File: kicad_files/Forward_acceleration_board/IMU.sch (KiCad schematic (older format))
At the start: 6 parts

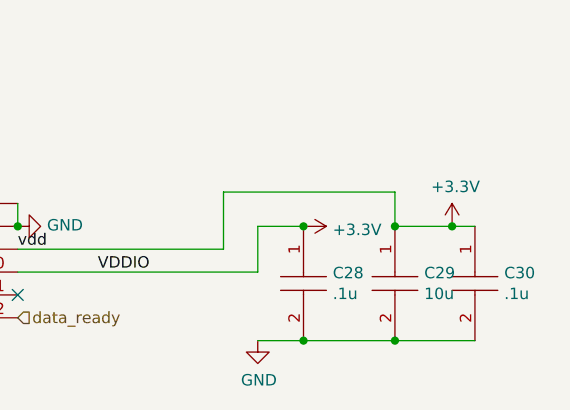
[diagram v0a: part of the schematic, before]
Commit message: updated BOMS for boards and added battery pack wiring schematic
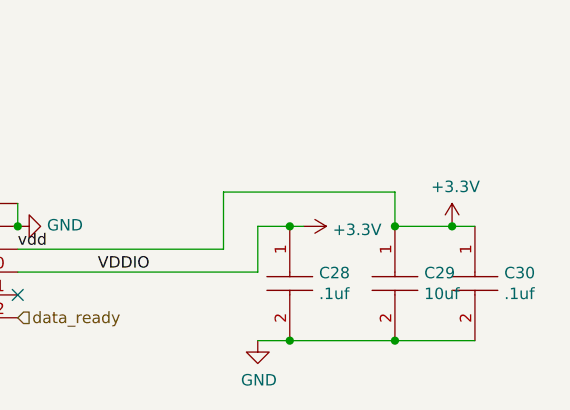
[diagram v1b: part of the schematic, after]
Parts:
- removed C28, C30: .1u, GRM155C91C105ME11J:CAPC1005X55N, symbol GRM155C80G106ME44D:GRM155C80G106ME44D
- removed C29: 10u, AS0805KKX7R0BB104:CAPC2012X145N, symbol AS0805KKX7R0BB104:AS0805KKX7R0BB104
- added C28, C30: .1uf, GRM155C91C105ME11J:CAPC1005X55N, symbol GRM155R62A104KE14D:GRM155R62A104KE14D
- added C29: 10uf, AS0805KKX7R0BB104:CAPC2012X145N, symbol GRM21BR61E106KA73K:GRM21BR61E106KA73K
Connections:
- net +3V3: now also C28.1, C29.1, C30.1
- net GND: now also C28.2, C29.2, C30.2
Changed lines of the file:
@@
 NoConn ~ 4550 3900
 $Comp
-L power:GND #PWR0152
+L Forward_acceleration_board-rescue:GND-power #PWR0152
 U 1 1 5D9F0090
 P 6050 3600
@@
 $EndComp
 $Comp
-L power:GND #PWR0153
+L Forward_acceleration_board-rescue:GND-power #PWR0153
 U 1 1 5D9F00CC
 P 4550 4000
@@
 data_ready
 $Comp
-L power:GND #PWR0154
+L Forward_acceleration_board-rescue:GND-power #PWR0154
 U 1 1 5DAEA2FA
 P 4550 3700
@@
 $EndComp
 $Comp
-L GRM155C80G106ME44D:GRM155C80G106ME44D C30
-U 1 1 5DAEA3F4
-P 8050 3600
-F 0 "C30" V 8254 3728 50  0000 L CNN
-F 1 ".1u" V 8345 3728 50  0000 L CNN
-F 2 "GRM155C91C105ME11J:CAPC1005X55N" H 8400 3650 50  0001 L CNN
-F 3 "https://componentsearchengine.com/Datasheets/1/GRM155C80G106ME44D.pdf" H 8400 3550 50  0001 L CNN
-F 4 "Multilayer Ceramic Capacitors MLCC - SMD/SMT 10UF      4V   20%        0402" H 8400 3450 50  0001 L CNN "Description"
-F 5 "0.55" H 8400 3350 50  0001 L CNN "Height"
-F 6 "81-GRM155C80G106ME44" H 8400 3250 50  0001 L CNN "Mouser Part Number"
-F 7 "https://www.mouser.com/Search/Refine.aspx?Keyword=81-GRM155C80G106ME44" H 8400 3150 50  0001 L CNN "Mouser Price/Stock"
-F 8 "Murata Electronics" H 8400 3050 50  0001 L CNN "Manufacturer_Name"
-F 9 "GRM155C80G106ME44D" H 8400 2950 50  0001 L CNN "Manufacturer_Part_Number"
-	1    8050 3600
-	0    1    1    0
-$EndComp
-$Comp
-L AS0805KKX7R0BB104:AS0805KKX7R0BB104 C29
-U 1 1 5DAEA659
-P 7700 3600
-F 0 "C29" V 7904 3728 50  0000 L CNN
-F 1 "10u" V 7995 3728 50  0000 L CNN
-F 2 "AS0805KKX7R0BB104:CAPC2012X145N" H 8050 3650 50  0001 L CNN
-F 3 "https://mouser.componentsearchengine.com/Datasheets/1/AS0805KKX7R0BB104.pdf" H 8050 3550 50  0001 L CNN
-F 4 "Multilayer Ceramic Capacitors MLCC - SMD/SMT 0.1uF 10% 100V AEC-Q200" H 8050 3450 50  0001 L CNN "Description"
-F 5 "1.45" H 8050 3350 50  0001 L CNN "Height"
-F 6 "YAGEO (PHYCOMP)" H 8050 3250 50  0001 L CNN "Manufacturer_Name"
-F 7 "AS0805KKX7R0BB104" H 8050 3150 50  0001 L CNN "Manufacturer_Part_Number"
-F 8 "603-AS0805KKX70BB104" H 8050 3050 50  0001 L CNN "Mouser Part Number"
-F 9 "https://www.mouser.com/Search/Refine.aspx?Keyword=603-AS0805KKX70BB104" H 8050 2950 50  0001 L CNN "Mouser Price/Stock"
-F 10 "" H 8050 2850 50  0001 L CNN "RS Part Number"
-F 11 "" H 8050 2750 50  0001 L CNN "RS Price/Stock"
-	1    7700 3600
-	0    1    1    0
-$EndComp
-$Comp
-L power:GND #PWR0155
+L Forward_acceleration_board-rescue:GND-power #PWR0155
 U 1 1 5DAEA827
 P 7100 4100
@@
 $EndComp
 Wire Wire Line
-	8050 4100 7700 4100
-Connection ~ 7700 4100
-Wire Wire Line
 	7100 3600 7100 3800
 Wire Wire Line
 	6050 3800 7100 3800
 Wire Wire Line
-	7100 3600 7300 3600
+	7100 3600 7240 3600
 Wire Wire Line
 	8050 3600 7950 3600
 $Comp
-L power:+3.3V #PWR0156
+L Forward_acceleration_board-rescue:+3.3V-power #PWR0156
 U 1 1 5DAEABD2
 P 7950 3600
@@
 Wire Wire Line
 	7700 3450 7700 3600
-Connection ~ 7700 3600
 $Comp
-L power:+3.3V #PWR0157
+L Forward_acceleration_board-rescue:+3.3V-power #PWR0157
 U 1 1 5DAEAD41
 P 7300 3600
@@
 $EndComp
 Wire Wire Line
-	7100 4100 7300 4100
+	7100 4100 7240 4100
 $Comp
-L GRM155C80G106ME44D:GRM155C80G106ME44D C28
-U 1 1 5D9EBE90
-P 7300 3600
-F 0 "C28" V 7504 3728 50  0000 L CNN
-F 1 ".1u" V 7595 3728 50  0000 L CNN
-F 2 "GRM155C91C105ME11J:CAPC1005X55N" H 7650 3650 50  0001 L CNN
-F 3 "https://componentsearchengine.com/Datasheets/1/GRM155C80G106ME44D.pdf" H 7650 3550 50  0001 L CNN
-F 4 "Multilayer Ceramic Capacitors MLCC - SMD/SMT 10UF      4V   20%        0402" H 7650 3450 50  0001 L CNN "Description"
-F 5 "0.55" H 7650 3350 50  0001 L CNN "Height"
-F 6 "81-GRM155C80G106ME44" H 7650 3250 50  0001 L CNN "Mouser Part Number"
-F 7 "https://www.mouser.com/Search/Refine.aspx?Keyword=81-GRM155C80G106ME44" H 7650 3150 50  0001 L CNN "Mouser Price/Stock"
-F 8 "Murata Electronics" H 7650 3050 50  0001 L CNN "Manufacturer_Name"
-F 9 "GRM155C80G106ME44D" H 7650 2950 50  0001 L CNN "Manufacturer_Part_Number"
-	1    7300 3600
+L GRM155R62A104KE14D:GRM155R62A104KE14D C30
+U 1 1 5DD4DCA5
+P 8050 3600
+F 0 "C30" V 8254 3728 50  0000 L CNN
+F 1 ".1uf" V 8345 3728 50  0000 L CNN
+F 2 "GRM155C91C105ME11J:CAPC1005X55N" H 8400 3650 50  0001 L CNN
+F 3 "https://componentsearchengine.com/Datasheets/1/GRM155R62A104KE14D.pdf" H 8400 3550 50  0001 L CNN
+F 4 "MURATA - GRM155R62A104KE14D - CAP, MLCC, X5R, 0.1UF, 100V, 0402" H 8400 3450 50  0001 L CNN "Description"
+F 5 "0.55" H 8400 3350 50  0001 L CNN "Height"
+F 6 "81-GRM155R62A104KE4D" H 8400 3250 50  0001 L CNN "Mouser Part Number"
+F 7 "https://www.mouser.com/Search/Refine.aspx?Keyword=81-GRM155R62A104KE4D" H 8400 3150 50  0001 L CNN "Mouser Price/Stock"
+F 8 "Murata Electronics" H 8400 3050 50  0001 L CNN "Manufacturer_Name"
+F 9 "GRM155R62A104KE14D" H 8400 2950 50  0001 L CNN "Manufacturer_Part_Number"
+	1    8050 3600
 	0    1    1    0
 $EndComp
-Connection ~ 7300 3600
-Connection ~ 7300 4100
+$Comp
+L GRM155R62A104KE14D:GRM155R62A104KE14D C28
+U 1 1 5DD4F3C8
+P 7240 3600
+F 0 "C28" V 7444 3728 50  0000 L CNN
+F 1 ".1uf" V 7535 3728 50  0000 L CNN
+F 2 "GRM155C91C105ME11J:CAPC1005X55N" H 7590 3650 50  0001 L CNN
+F 3 "https://componentsearchengine.com/Datasheets/1/GRM155R62A104KE14D.pdf" H 7590 3550 50  0001 L CNN
+F 4 "MURATA - GRM155R62A104KE14D - CAP, MLCC, X5R, 0.1UF, 100V, 0402" H 7590 3450 50  0001 L CNN "Description"
+F 5 "0.55" H 7590 3350 50  0001 L CNN "Height"
+F 6 "81-GRM155R62A104KE4D" H 7590 3250 50  0001 L CNN "Mouser Part Number"
+F 7 "https://www.mouser.com/Search/Refine.aspx?Keyword=81-GRM155R62A104KE4D" H 7590 3150 50  0001 L CNN "Mouser Price/Stock"
+F 8 "Murata Electronics" H 7590 3050 50  0001 L CNN "Manufacturer_Name"
+F 9 "GRM155R62A104KE14D" H 7590 2950 50  0001 L CNN "Manufacturer_Part_Number"
+	1    7240 3600
+	0    1    1    0
+$EndComp
+Connection ~ 7240 3600
 Wire Wire Line
-	7300 4100 7700 4100
+	7240 3600 7300 3600
+Connection ~ 7240 4100
+Wire Wire Line
+	7240 4100 7700 4100
+$Comp
+L GRM21BR61E106KA73K:GRM21BR61E106KA73K C29
+U 1 1 5DD50833
+P 7700 3600
+F 0 "C29" V 7904 3728 50  0000 L CNN
+F 1 "10uf" V 7995 3728 50  0000 L CNN
+F 2 "AS0805KKX7R0BB104:CAPC2012X145N" H 8050 3650 50  0001 L CNN
+F 3 "https://componentsearchengine.com/Datasheets/1/GRM21BR61E106KA73K.pdf" H 8050 3550 50  0001 L CNN
+F 4 "Capacitor GRM21_0.15 L=2.0mm W=1.25mm T=1.25mm" H 8050 3450 50  0001 L CNN "Description"
+F 5 "1.45" H 8050 3350 50  0001 L CNN "Height"
+F 6 "81-GRM21BR61E106KA3K" H 8050 3250 50  0001 L CNN "Mouser Part Number"
+F 7 "https://www.mouser.com/Search/Refine.aspx?Keyword=81-GRM21BR61E106KA3K" H 8050 3150 50  0001 L CNN "Mouser Price/Stock"
+F 8 "Murata Electronics" H 8050 3050 50  0001 L CNN "Manufacturer_Name"
+F 9 "GRM21BR61E106KA73K" H 8050 2950 50  0001 L CNN "Manufacturer_Part_Number"
+	1    7700 3600
+	0    1    1    0
+$EndComp
+Connection ~ 7700 3600
+Connection ~ 7700 4100
+Wire Wire Line
+	7700 4100 8050 4100
 $EndSCHEMATC
